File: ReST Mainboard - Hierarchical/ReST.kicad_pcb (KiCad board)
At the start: 2 copper layers, 100 x 100 mm, 157 parts, among them IC1 AT24C256, P1 CONN_01X02, P10 CONN_02X04, P11 CONN_01X04, P12 CONN_01X04, P13 CONN_01X04, P14 CONN_01X04, P15 USB_OTG, P16 CONN_02X05, P17 CONN_02X05, P18 CONN_02X05, P19 CONN_01X04, P2 CONN_01X03, P20 CONN_01X02, P21 CONN_01X04, P22 CONN_02X03, P23 CONN_02X03, P24 CONN_01X04, P25 CONN_02X03, P26 CONN_02X03, P27 CONN_02X06, P28 CONN_02X02, P29 CONN_01X02, P3 CONN_01X02, P30 CONN_01X02, P31 CONN_01X02, P32 CONN_02X02, P33 CONN_02X02, P34 CONN_02X02, P4 CONN_01X03, P5 CONN_01X03, P6 CONN_01X03, P7 CONN_01X03, P8 CONN_01X03, P9 CONN_01X03, Q1 TBD, Q10 Q_AOT240L, Q11 Q_AOT240L, Q12 Q_AOT240L, Q2 TBD, Q3 TBD, Q4 TBD, Q7 Q_BSH105/IRLML2502, Q8 Q_BSH105/IRLML2502, Q9 Q_BSH105/IRLML2502, U1 MCP23017, U10 USBLC6-2, U2 POLOLU_A4988, U3 ACT4088, U4 SC4626, U5 POLOLU_A4988, U6 POLOLU_A4988, U7 POLOLU_A4988, U8 POLOLU_A4988, U9 STM32F10x/STM32F4x, X1 Crystal_Small

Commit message: started routing
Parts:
- moved F2 13.6 mm to (57.0, 162.1)
- moved R9 12.8 mm to (111.2, 155.2), turned to 0 degrees
- moved R41 12.8 mm to (73.5, 146.8)
- moved R42 11.8 mm to (85.5, 146.8)
- moved D3 11.8 mm to (59.6, 156.2), turned to 270 degrees
- moved R38 11.2 mm to (68.8, 139.8)
- moved R43 10.9 mm to (97.5, 146.8)
- moved R39 10.6 mm to (80.8, 139.8)
- moved D1 10.0 mm to (21.6, 154.2), turned to 90 degrees
- moved R5 10.0 mm to (30.7, 146.7), turned to 0 degrees
- moved R40 10.00 mm to (92.8, 139.8)
- moved P19 8.68 mm to (67.0, 100.6), turned to 180 degrees
- moved R2 8.23 mm to (30.7, 100.2), turned to 0 degrees
- moved R3 8.23 mm to (30.7, 115.7), turned to 0 degrees
- moved R1 8.23 mm to (30.7, 131.2), turned to 0 degrees
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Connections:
- net /Logic/USB_D+ renamed /Logic/USBP_D+
- net /Logic/USB_D- renamed /Logic/USBP_D-
- net Net-(P10-Pad1) renamed /Stepper and Endstop/Z_1B
- net Net-(P10-Pad3) renamed /Stepper and Endstop/Z_1A
- net Net-(P10-Pad5) renamed /Stepper and Endstop/Z_2A
- net Net-(P10-Pad7) renamed /Stepper and Endstop/Z_2B
- net Net-(P11-Pad1) renamed /Stepper and Endstop/E0_2B
- net Net-(P11-Pad2) renamed /Stepper and Endstop/E0_2A
- net Net-(P11-Pad3) renamed /Stepper and Endstop/E0_1A
- net Net-(P11-Pad4) renamed /Stepper and Endstop/E0_1B
- net Net-(P12-Pad1) renamed /Stepper and Endstop/Y_2B
- net Net-(P12-Pad2) renamed /Stepper and Endstop/Y_2A
- net Net-(P12-Pad3) renamed /Stepper and Endstop/Y_1A
- net Net-(P12-Pad4) renamed /Stepper and Endstop/Y_1B
- net Net-(P13-Pad1) renamed /Stepper and Endstop/X_2B
- net Net-(P13-Pad2) renamed /Stepper and Endstop/X_2A
- net Net-(P13-Pad3) renamed /Stepper and Endstop/X_1A
- net Net-(P13-Pad4) renamed /Stepper and Endstop/X_1B
- net Net-(P14-Pad1) renamed /Stepper and Endstop/E1_2B
- net Net-(P14-Pad2) renamed /Stepper and Endstop/E1_2A
- net Net-(P14-Pad3) renamed /Stepper and Endstop/E1_1A
- net Net-(P14-Pad4) renamed /Stepper and Endstop/E1_1B
- net Net-(Q11-Pad1) renamed /Heater/H1_GATE
- net USB_DM_- renamed USB_MCU-
- net USB_DP_+ renamed USB_MCU+
- C36 pad 1: TEMP_0 -> TEMP_1
- C37 pad 1: TEMP_1 -> TEMP_0
- P26 pad 1: +5V -> +3V3
- P26 pad 2: +3V3 -> +5V
- P26 pad 3: +5V -> +3V3
- P26 pad 4: +3V3 -> +5V
- P26 pad 5: +5V -> +3V3
- P26 pad 6: +3V3 -> +5V
- P3 pad 1: /Power Input/12VA-R -> GND
- P3 pad 2: GND -> /Power Input/12VA-R
- Q10 pad 1: Net-(Q10-Pad1) -> /Heater/H2_GATE
- Q12 pad 1: Net-(Q12-Pad1) -> /Heater/H2_GATE
- R41 pad 2: Net-(Q10-Pad1) -> /Heater/H2_GATE
- R43 pad 2: Net-(Q12-Pad1) -> /Heater/H2_GATE
- U1 pad 24: /Stepper and Endstop/YM1 -> /Stepper and Endstop/YM3
- U1 pad 26: /Stepper and Endstop/YM3 -> /Stepper and Endstop/YM1
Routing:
- net +12V: track 0.00 -> 236.1 mm, vias 0 -> 2
- net STEPPER_Z_EN: track 0.00 -> 58.7 mm
- net STEPPER_X_EN: track 0.00 -> 53.2 mm
- net STEPPER_Y_EN: track 0.00 -> 49.3 mm
- net /Stepper and Endstop/ZM1: track 0.00 -> 47.3 mm, vias 0 -> 3
- net STEPPER_Z_STEP: track 0.00 -> 40.5 mm
- net /Stepper and Endstop/ZM2: track 0.00 -> 40.0 mm, vias 0 -> 3
- net /Stepper and Endstop/ZM3: track 0.00 -> 37.6 mm, vias 0 -> 3
- net STEPPER_X_STEP: track 0.00 -> 36.6 mm
- net STEPPER_Z_DIR: track 0.00 -> 36.2 mm
- net STEPPER_X_DIR: track 0.00 -> 33.9 mm
- net +3V3: track 0.00 -> 33.8 mm
- net STEPPER_Y_STEP: track 0.00 -> 31.8 mm
- net +5V: track 0.00 -> 30.3 mm
- net STEPPER_Y_DIR: track 0.00 -> 29.1 mm
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- added copper zone on B.Cu, net +12V
- added copper zone on F.Cu, net +12V
- added copper zone on B.Cu, net +12VA
- added copper zone on F.Cu, net +12VA
- added copper zone on B.Cu, net /Heater/HEATER_0_OUT
- added copper zone on F.Cu, net /Heater/HEATER_0_OUT
- added copper zone on B.Cu, net /Heater/HEATER_1_OUT
- added copper zone on F.Cu, net /Heater/HEATER_1_OUT
- added copper zone on B.Cu, net /Heater/HEATER_2_OUT
- added copper zone on F.Cu, net /Heater/HEATER_2_OUT
- added copper zone on B.Cu, net /Power Input/12V-R
- added copper zone on F.Cu, net /Power Input/12V-R
- added copper zone on B.Cu, net /Power Input/12VA-R
- added copper zone on F.Cu, net /Power Input/12VA-R
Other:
- net class Stepperdriver added: clearance 0.5, trace_width 0.3, via_dia 0.6, via_drill 0.4

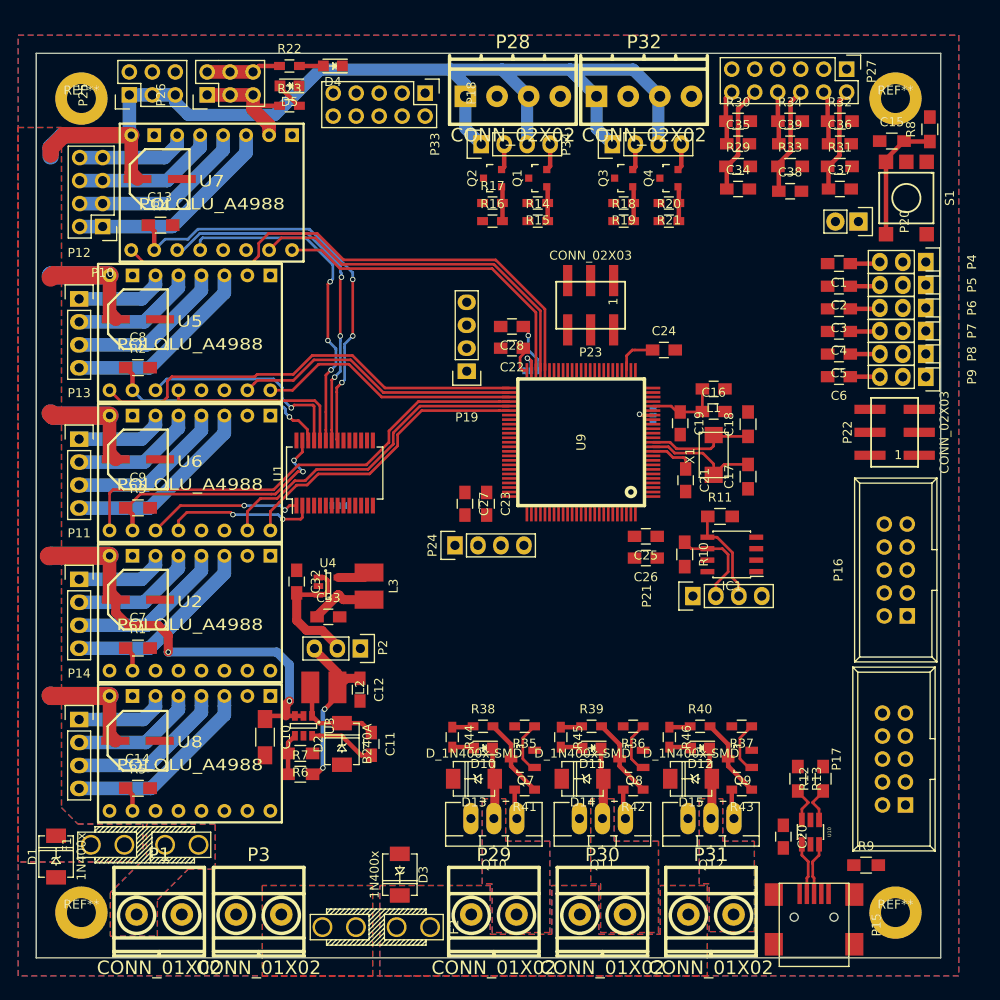
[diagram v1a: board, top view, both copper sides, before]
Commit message: Mostly finished with main PCB. Only need to work the High Current Stuff out. On Vacation for now
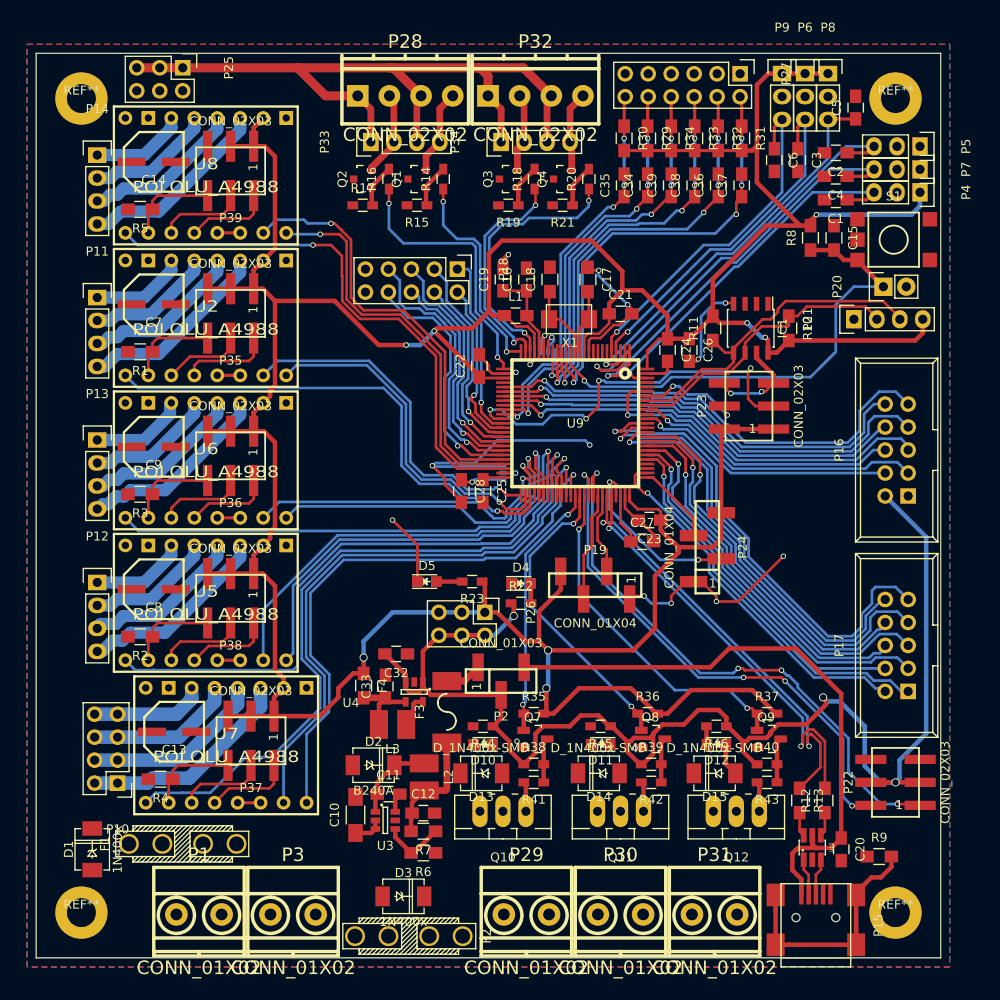
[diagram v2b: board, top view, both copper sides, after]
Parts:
- removed JP1: JUMPER3, ReST-Library:S_JUMPER_3
- removed U1: MCP23017, Housings_SSOP:SSOP-28_5.3x10.2mm_Pitch0.65mm
- added F3: F_Small, ReST-Library:FUSE-1812, F.Cu at (64.8, 138.2)
- added F4: F_Small, Resistors_SMD:R_0805_HandSoldering, F.Cu at (55.6, 135.3)
- added P35: CONN_02X03, ReST-Library:bb02-hp06, F.Cu at (41.0, 94.2)
- added P36: CONN_02X03, ReST-Library:bb02-hp06, F.Cu at (41.0, 110.0)
- added P37: CONN_02X03, ReST-Library:bb02-hp06, F.Cu at (43.2, 141.4)
- added P38: CONN_02X03, ReST-Library:bb02-hp06, F.Cu at (41.0, 125.7)
- added P39: CONN_02X03, ReST-Library:bb02-hp06, F.Cu at (41.0, 78.5)
- P19, P24: footprint Pin_Headers:Pin_Header_Straight_1x04 -> ReST-Library:bb02-hy04a
- P2: footprint Pin_Headers:Pin_Header_Straight_1x03 -> ReST-Library:bb02-hy03a
- moved P26 64.9 mm to (69.0, 127.2), turned to 270 degrees
- moved R22 64.7 mm to (73.0, 126.2)
- moved C14 64.0 mm to (32.5, 77.5)
- moved R5 64.0 mm to (30.9, 82.7), turned to 180 degrees
- moved U8 63.9 mm to (38.2, 79.0)
- moved P14 62.4 mm to (26.2, 76.7)
- moved P10 61.6 mm to (28.4, 146.1)
- moved R4 61.2 mm to (33.2, 145.7), turned to 180 degrees
- moved C13 61.1 mm to (34.7, 140.4)
- moved U7 61.1 mm to (40.5, 141.9)
- moved D4 60.9 mm to (73.0, 124.0), turned to 0 degrees
- moved D5 56.9 mm to (62.6, 123.8), turned to 0 degrees
- moved R23 56.3 mm to (67.7, 123.8), turned to 180 degrees
- moved P22 38.7 mm to (114.5, 146.1)
- moved P9 37.1 mm to (101.9, 67.7), turned to 0 degrees
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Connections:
- C12 pad 1: VEE -> Net-(C12-Pad1)
- C33 pad 1: +3V3 -> Net-(C33-Pad1)
- L2 pad 2: VEE -> Net-(C12-Pad1)
- L3 pad 2: +3V3 -> Net-(C33-Pad1)
- P16 pad 10: DISPLAY_RD -> SPI_MISO
- P16 pad 3: SPI_SCK -> DISPLAY_RD
- P16 pad 4: DISPLAY_EXTRA_0 -> DISPLAY_WR
- P16 pad 5: SPI_MISO -> SPI_CS2
- P16 pad 6: SPI_CS1 -> DISPLAY_EXTRA_0
- P16 pad 8: SPI_CS2 -> SPI_CS1
- P16 pad 9: DISPLAY_WR -> SPI_SCK
- P17 pad 1: DISPLAY_D1 -> DISPLAY_CS
- P17 pad 10: DISPLAY_CS -> DISPLAY_D6
- P17 pad 2: DISPLAY_D0 -> DISPLAY_CD
- P17 pad 3: DISPLAY_D3 -> DISPLAY_D1
- P17 pad 4: DISPLAY_D2 -> DISPLAY_D0
- P17 pad 5: DISPLAY_D5 -> DISPLAY_D3
- P17 pad 6: DISPLAY_D4 -> DISPLAY_D2
- P17 pad 7: DISPLAY_D7 -> DISPLAY_D5
- P17 pad 8: DISPLAY_D6 -> DISPLAY_D4
- P17 pad 9: DISPLAY_CD -> DISPLAY_D7
- P2 pad 1: VCC -> VEE
- P2 pad 3: VEE -> VCC
- P23 pad 3: BOOT_0 -> BOOT_1
- P23 pad 4: BOOT_1 -> BOOT_0
- R7 pad 2: VEE -> Net-(C12-Pad1)
- S1 pad 1: RESET -> (no net)
- U4 pad 4: +3V3 -> Net-(C33-Pad1)
- U9 pad 23: EXTRA_0 -> EXTRA_3
- U9 pad 24: EXTRA_1 -> EXTRA_2
- U9 pad 25: EXTRA_2 -> EXTRA_1
- U9 pad 26: EXTRA_3 -> EXTRA_0
- U9 pad 46: STEPPER_Z_EN -> STEPPER_E_1_STEP
- U9 pad 47: STEPPER_Z_STEP -> STEPPER_E_1_DIR
- U9 pad 48: STEPPER_Z_DIR -> STEPPER_E_1_EN
- U9 pad 51: STEPPER_Y_EN -> STEPPER_E_0_STEP
- U9 pad 52: STEPPER_Y_STEP -> STEPPER_E_0_DIR
- U9 pad 53: STEPPER_Y_DIR -> STEPPER_E_0_EN
- U9 pad 54: STEPPER_X_EN -> STEPPER_X_STEP
- U9 pad 55: STEPPER_X_STEP -> STEPPER_X_DIR
- U9 pad 56: STEPPER_X_DIR -> STEPPER_X_EN
- U9 pad 57: STEPPER_E_0_EN -> STEPPER_Y_STEP
- U9 pad 58: STEPPER_E_0_STEP -> STEPPER_Y_DIR
- U9 pad 59: STEPPER_E_0_DIR -> STEPPER_Y_EN
- U9 pad 60: STEPPER_E_1_EN -> STEPPER_Z_EN
- U9 pad 61: STEPPER_E_1_STEP -> STEPPER_Z_STEP
- U9 pad 62: STEPPER_E_1_DIR -> STEPPER_Z_DIR
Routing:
- net +3V3: track 33.8 -> 452.5 mm, vias 0 -> 9
- net +12V: track 236.1 -> 89.6 mm, vias 2 -> 0
- net +5V: track 30.3 -> 152.6 mm, vias 0 -> 3
- net GND: track 0.00 -> 120.6 mm, vias 0 -> 18
- net VCC: track 0.00 -> 66.5 mm
- net SERVO_1: track 0.00 -> 63.0 mm, vias 0 -> 4
- net STEPPER_E_1_EN: track 0.00 -> 61.4 mm, vias 0 -> 1
- net SERVO_0: track 0.00 -> 58.8 mm, vias 0 -> 4
- net STEPPER_E_0_EN: track 0.00 -> 56.5 mm, vias 0 -> 1
- net DISPLAY_D7: track 0.00 -> 54.1 mm, vias 0 -> 1
- net SPI_SCK: track 0.00 -> 52.0 mm, vias 0 -> 1
- net SPI_MOSI: track 0.00 -> 50.1 mm, vias 0 -> 1
- net SPI_CS2: track 0.00 -> 49.6 mm, vias 0 -> 1
- net DISPLAY_D5: track 0.00 -> 49.2 mm, vias 0 -> 1
- net DISPLAY_D6: track 0.00 -> 48.8 mm, vias 0 -> 1
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- removed copper zone on B.Cu, net +12V
- removed copper zone on F.Cu, net +12V
- removed copper zone on B.Cu, net +12VA
- removed copper zone on F.Cu, net +12VA
- removed copper zone on B.Cu, net /Heater/HEATER_0_OUT
- removed copper zone on F.Cu, net /Heater/HEATER_0_OUT
- removed copper zone on B.Cu, net /Heater/HEATER_1_OUT
- removed copper zone on F.Cu, net /Heater/HEATER_1_OUT
- removed copper zone on B.Cu, net /Heater/HEATER_2_OUT
- removed copper zone on F.Cu, net /Heater/HEATER_2_OUT
- removed copper zone on B.Cu, net /Power Input/12V-R
- removed copper zone on F.Cu, net /Power Input/12V-R
- removed copper zone on B.Cu, net /Power Input/12VA-R
- removed copper zone on F.Cu, net /Power Input/12VA-R

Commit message: electrically finished. in the works of the silkscreening.
Schematic for SD Card Adapter and a RepRapDiscount-Adapter in the works. but not in this commit
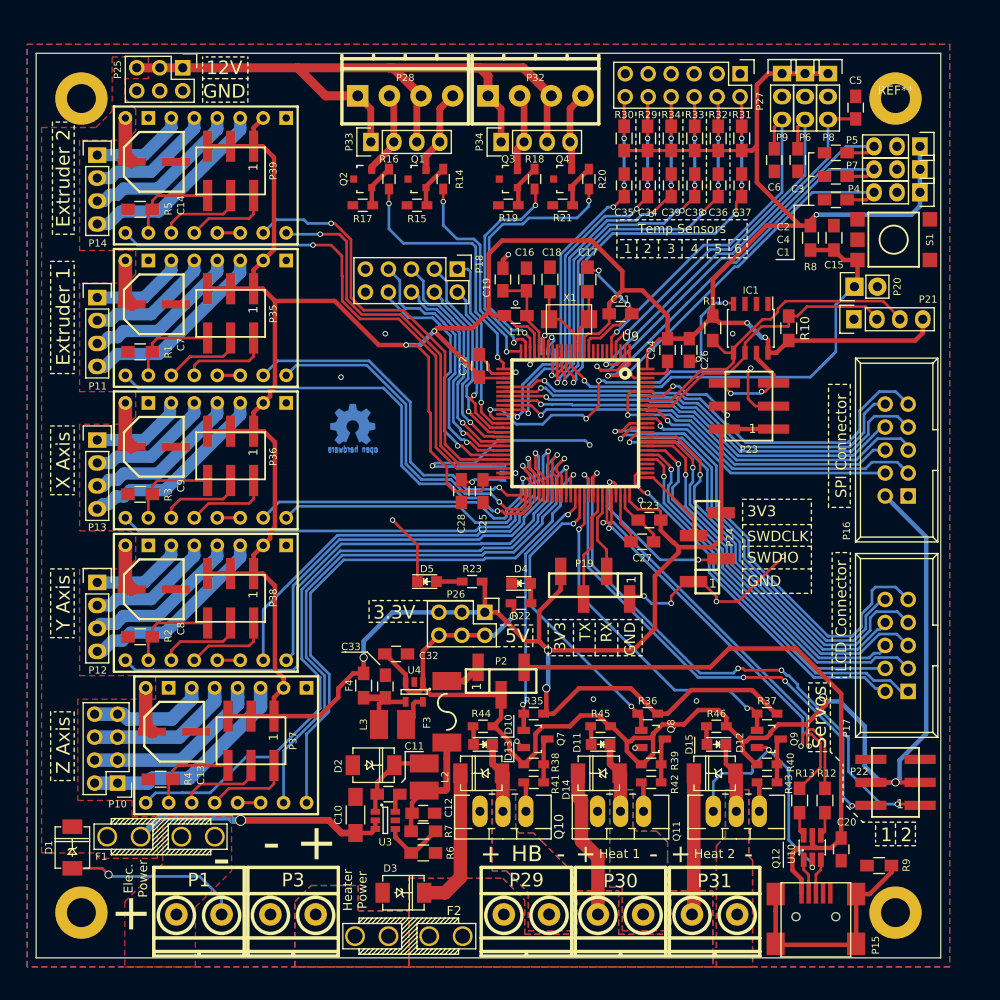
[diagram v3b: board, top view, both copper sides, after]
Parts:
- added G***: LOGO, ReST-Library:Logo_copper_OSHW_6x6mm, B.Cu at (54.5, 106.5)
- added G***: LOGO, ReST-Library:STM32, B.Cu at (54.5, 112.5)
- added G***: LOGO, ReST-Library:Logo_silk_OSHW_6x6mm, B.Cu at (54.5, 106.5)
- P15: footprint Connect:USB_Mini-B -> ReST-Library:USB_Mini-B
- U9: value STM32F10x/STM32F4x -> STM32F1/STM32F4
- moved P20 3.20 mm to (109.9, 91.2)
- moved F1 2.53 mm to (33.2, 152.1)
- moved D1 2.21 mm to (23.4, 153.2)
- moved R9 1.00 mm to (112.7, 155.2)
- moved D3 0.40 mm to (60.0, 158.2)
- moved P15 0.10 mm to (105.7, 161.8)
- renumbered U2 to ?, U5 to ?, U6 to ?, U7 to ?, U8 to ?
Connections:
- Q10 pad 1: /Heater/H2_GATE -> /Heater/H0_GATE
- R41 pad 2: /Heater/H2_GATE -> /Heater/H0_GATE
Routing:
- net +12V: track 89.6 -> 140.7 mm, vias 0 -> 1
- net +12VA: track 0.00 -> 48.4 mm
- net GND: track 120.6 -> 163.5 mm, vias 18 -> 21
- net +3V3: track 452.5 -> 483.3 mm
- net /Heater/HEATER_1_OUT: track 0.00 -> 7.88 mm
- net /Heater/HEATER_0_OUT: track 0.00 -> 7.88 mm
- net /Heater/HEATER_2_OUT: track 3.64 -> 7.88 mm
- net RESET: track 56.9 -> 52.7 mm
- net /Heater/H2_GATE: track 6.60 -> 3.30 mm
- net /Heater/H0_GATE: track 0.00 -> 3.30 mm
- net Net-(D11-Pad2): track 0.07 -> 2.09 mm
- net Net-(D10-Pad2): track 0.00 -> 2.02 mm
- net Net-(P15-Pad6): track 26.4 -> 25.5 mm
- net (no net): vias 0 -> 7
- added copper zone on F.Cu, net +12V
- added copper zone on B.Cu, net +12VA
- added copper zone on F.Cu, net +12VA
- added copper zone on B.Cu, net /Heater/HEATER_0_OUT
- added copper zone on F.Cu, net /Heater/HEATER_0_OUT
- added copper zone on B.Cu, net /Heater/HEATER_1_OUT
- added copper zone on F.Cu, net /Heater/HEATER_1_OUT
- added copper zone on B.Cu, net /Heater/HEATER_2_OUT
- added copper zone on F.Cu, net /Heater/HEATER_2_OUT
- added copper zone on F.Cu, net /Power Input/12V-R
- added copper zone on B.Cu, net /Power Input/12VA-R
- added copper zone on F.Cu, net /Power Input/12VA-R
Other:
- board text added: "+"
- board text added: "-"
- board text added: "1"
- board text added: "12V"
- board text added: "2"
- board text added: "3"
- board text added: "3.3V"
- board text added: "3V3"
- board text added: "4"
- board text added: "5"
- board text added: "5V"
- board text added: "6"
- board text added: "Elec. Power"
- board text added: "Extruder 1"
- board text added: "Extruder 2"
- board text added: "GND"
- board text added: "HB"
- board text added: "Heat 1"
- board text added: "Heat 2"
- board text added: "Heater Power"
- board text added: "LCD Connector"
- board text added: "RX"
- board text added: "SPI Connector"
- board text added: "SWDCLK"
- board text added: "SWDIO"
- board text added: "Servos"
- board text added: "TX"
- board text added: "Temp Sensors"
- board text added: "X Axis"
- board text added: "Y Axis"
- board text added: "Z Axis"

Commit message: final release of the main PCB
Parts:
- removed the G*** at (54.5, 106.5)
- removed the G*** at (54.5, 112.5)
- added G***: LOGO, ReST-Library:STM32-6mm, B.Cu at (86.2, 132.4)
- moved G*** 48.3 mm to (95.5, 131.8)
- moved JP3 0.28 mm to (75.8, 98.2)
- moved JP2 0.10 mm to (71.0, 111.8)
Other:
- board text added: "0"
- board text added: "7"
- board text added: "8"
- board text added: "BOOT0"
- board text added: "BOOT1"
- board text added: "EXT"
- board text added: "Endstops"
- board text added: "Extra Power Output"
- board text added: "F1: JP2: 0 JP3: 0 No CAP C27"
- board text added: "F4: JP2: 1 JP3: 1 CAP C27"
- board text added: "Fuse for Electronics and Stepper: 7.5A Fuse should be enough"
- board text added: "Fuse for Heatbed and Heaters. 150W HB+40W Heater : 20A Fuse 150W HB+2x40W Heater : 25A Fuse"
- board text added: "Github: berryelectronics/Rest32"
- board text added: "Input: 12-24V 5A - 35A Reverse Polarity Protection Output: 5V 1.5A & 3V 1A"
- board text added: "MCU Config"
- board text added: "Microstepping: Jumper for ON No Jumper for OFF Look up MS Setting for your Driver"
- board text added: "OUT 1"
- board text added: "OUT 2"
- board text added: "OUT 3"
- board text added: "OUT 4"
- board text added: "P2: Select Logic Supply"
- board text added: "RST"
- board text added: "RepRap STM32-based Controller Board"
- board text added: "SCL"
- board text added: "SDA"
- board text added: "USB"
- board text added: "User Pins"
- board text added: "Website: www.rest32.tk"
- board text added: "X Max"
- board text added: "X Min"
- board text added: "Y Max"
- board text added: "Y Min"
- board text added: "Z Max"
- board text added: "Z Min"
